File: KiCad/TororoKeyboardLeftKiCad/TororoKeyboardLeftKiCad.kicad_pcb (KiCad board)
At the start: 2 copper layers, 142.1 x 99.2 mm, 97 parts, among them J1 MJ-4PP-9, SW1 SW_PUSH, SW10 SW_PUSH, SW11 SW_PUSH, SW12 SW_PUSH, SW13 SW_PUSH, SW14 SW_PUSH, SW15 SW_PUSH, SW16 SW_PUSH, SW17 SW_PUSH, SW18 SW_PUSH, SW19 SW_PUSH, SW2 SW_PUSH, SW20 SW_PUSH, SW21 SW_PUSH, SW22 SW_PUSH, SW23 SW_PUSH, SW24 SW_PUSH, SW25 SW_PUSH, SW26 SW_PUSH, SW27 SW_PUSH, SW28 SW_PUSH, SW29 SW_PUSH, SW3 SW_PUSH, SW4 SW_PUSH, SW5 SW_PUSH, SW6 SW_PUSH, SW7 SW_PUSH, SW8 SW_PUSH, SW9 SW_PUSH, U1 ProMicro

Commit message: レイアウトを微調整
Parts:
- moved U1 0.30 mm to (51.1, 46.4)
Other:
- board size 142.1 x 99.2 mm -> 139.7 x 99.2 mm
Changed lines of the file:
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@@
   (general
     (thickness 1.6)
-    (drawings 266)
+    (drawings 268)
     (tracks 0)
     (zones 0)
@@
     (add_net row5)
   )
+  (module kbd_tororo:Hybrid_PCB_100H_no-silk_no_ref (layer F.Cu)
+    (at 66.675 47.625)
+    (fp_text reference SW2 (at 0 3.175) (layer F.SilkS) hide
+      (effects (font (size 1.27 1.524) (thickness 0.2032)))
+    )
+    (fp_text value SW_PUSH (at 0 5.08) (layer F.SilkS) hide
+      (effects (font (size 1.27 1.524) (thickness 0.2032)))
+    )
+    (fp_line (start -6.985 6.985) (end -6.985 -6.985) (layer Eco2.User) (width 0.1524))
+    (fp_line (start 6.985 6.985) (end -6.985 6.985) (layer Eco2.User) (width 0.1524))
+    (fp_line (start 6.985 -6.985) (end 6.985 6.985) (layer Eco2.User) (width 0.1524))
+    (fp_line (start -6.985 -6.985) (end 6.985 -6.985) (layer Eco2.User) (width 0.1524))
+    (fp_line (start -9.398 9.398) (end -9.398 -9.398) (layer Dwgs.User) (width 0.1524))
+    (fp_line (start 9.398 9.398) (end -9.398 9.398) (layer Dwgs.User) (width 0.1524))
+    (fp_line (start 9.398 -9.398) (end 9.398 9.398) (layer Dwgs.User) (width 0.1524))
+    (fp_line (start -9.398 -9.398) (end 9.398 -9.398) (layer Dwgs.User) (width 0.1524))
+    (fp_line (start -6.35 6.35) (end -6.35 -6.35) (layer Cmts.User) (width 0.1524))
+    (fp_line (start 6.35 6.35) (end -6.35 6.35) (layer Cmts.User) (width 0.1524))
+    (fp_line (start 6.35 -6.35) (end 6.35 6.35) (layer Cmts.User) (width 0.1524))
+    (fp_line (start -6.35 -6.35) (end 6.35 -6.35) (layer Cmts.User) (width 0.1524))
+    (fp_text user 1.00u (at -5.715 8.255) (layer Dwgs.User) hide
+      (effects (font (size 1.524 1.524) (thickness 0.3048)))
+    )
+    (pad 1 thru_hole oval (at -3.155 -3.27 138.1) (size 2.5 4.461556) (drill 0.001) (layers *.Cu *.Mask)
+      (net 71 col2))
+    (pad 1 thru_hole circle (at -3.81 -2.54 330.95) (size 2 2) (drill 1.524) (layers *.Cu *.Mask)
+      (net 71 col2))
+    (pad "" np_thru_hole circle (at 5.08 0 90) (size 1.8 1.8) (drill 1.8) (layers *.Cu *.Mask))
+    (pad "" np_thru_hole circle (at -5.08 0 90) (size 1.8 1.8) (drill 1.8) (layers *.Cu *.Mask))
+    (pad "" np_thru_hole circle (at 0 0 90) (size 3.9878 3.9878) (drill 3.9878) (layers *.Cu *.Mask))
+    (pad 1 thru_hole circle (at -2.5 -4 330.95) (size 2 2) (drill 1.524) (layers *.Cu *.Mask)
+      (net 71 col2))
+    (pad 2 thru_hole circle (at 2.54 -5.08 330.95) (size 2 2) (drill 1.524) (layers *.Cu *.Mask)
+      (net 3 "Net-(D2-Pad2)"))
+    (pad 2 thru_hole circle (at 2.5 -4.5 330.95) (size 2 2) (drill 1.524) (layers *.Cu *.Mask)
+      (net 3 "Net-(D2-Pad2)"))
+    (pad 2 thru_hole oval (at 2.52 -4.79 356.055) (size 2.5 3.081378) (drill 0.001) (layers *.Cu *.Mask)
+      (net 3 "Net-(D2-Pad2)"))
+  )
   (module kbd:HOLE (layer F.Cu)
     (at 157.1625 114.3)
@@
   )
   (module kbd_tororo:Hybrid_PCB_100H_no-silk_no_ref (layer F.Cu)
-    (at 66.675 47.625)
-    (fp_text reference SW2 (at 0 3.175) (layer F.SilkS) hide
-      (effects (font (size 1.27 1.524) (thickness 0.2032)))
-    )
-    (fp_text value SW_PUSH (at 0 5.08) (layer F.SilkS) hide
-      (effects (font (size 1.27 1.524) (thickness 0.2032)))
-    )
-    (fp_line (start -6.985 6.985) (end -6.985 -6.985) (layer Eco2.User) (width 0.1524))
-    (fp_line (start 6.985 6.985) (end -6.985 6.985) (layer Eco2.User) (width 0.1524))
-    (fp_line (start 6.985 -6.985) (end 6.985 6.985) (layer Eco2.User) (width 0.1524))
-    (fp_line (start -6.985 -6.985) (end 6.985 -6.985) (layer Eco2.User) (width 0.1524))
-    (fp_line (start -9.398 9.398) (end -9.398 -9.398) (layer Dwgs.User) (width 0.1524))
-    (fp_line (start 9.398 9.398) (end -9.398 9.398) (layer Dwgs.User) (width 0.1524))
-    (fp_line (start 9.398 -9.398) (end 9.398 9.398) (layer Dwgs.User) (width 0.1524))
-    (fp_line (start -9.398 -9.398) (end 9.398 -9.398) (layer Dwgs.User) (width 0.1524))
-    (fp_line (start -6.35 6.35) (end -6.35 -6.35) (layer Cmts.User) (width 0.1524))
-    (fp_line (start 6.35 6.35) (end -6.35 6.35) (layer Cmts.User) (width 0.1524))
-    (fp_line (start 6.35 -6.35) (end 6.35 6.35) (layer Cmts.User) (width 0.1524))
-    (fp_line (start -6.35 -6.35) (end 6.35 -6.35) (layer Cmts.User) (width 0.1524))
-    (fp_text user 1.00u (at -5.715 8.255) (layer Dwgs.User) hide
-      (effects (font (size 1.524 1.524) (thickness 0.3048)))
-    )
-    (pad 1 thru_hole oval (at -3.155 -3.27 138.1) (size 2.5 4.461556) (drill 0.001) (layers *.Cu *.Mask)
-      (net 71 col2))
-    (pad 1 thru_hole circle (at -3.81 -2.54 330.95) (size 2 2) (drill 1.524) (layers *.Cu *.Mask)
-      (net 71 col2))
-    (pad "" np_thru_hole circle (at 5.08 0 90) (size 1.8 1.8) (drill 1.8) (layers *.Cu *.Mask))
-    (pad "" np_thru_hole circle (at -5.08 0 90) (size 1.8 1.8) (drill 1.8) (layers *.Cu *.Mask))
-    (pad "" np_thru_hole circle (at 0 0 90) (size 3.9878 3.9878) (drill 3.9878) (layers *.Cu *.Mask))
-    (pad 1 thru_hole circle (at -2.5 -4 330.95) (size 2 2) (drill 1.524) (layers *.Cu *.Mask)
-      (net 71 col2))
-    (pad 2 thru_hole circle (at 2.54 -5.08 330.95) (size 2 2) (drill 1.524) (layers *.Cu *.Mask)
-      (net 3 "Net-(D2-Pad2)"))
-    (pad 2 thru_hole circle (at 2.5 -4.5 330.95) (size 2 2) (drill 1.524) (layers *.Cu *.Mask)
-      (net 3 "Net-(D2-Pad2)"))
-    (pad 2 thru_hole oval (at 2.52 -4.79 356.055) (size 2.5 3.081378) (drill 0.001) (layers *.Cu *.Mask)
-      (net 3 "Net-(D2-Pad2)"))
-  )
-  (module kbd_tororo:Hybrid_PCB_100H_no-silk_no_ref (layer F.Cu)
     (at 52.3875 66.675)
     (fp_text reference SW3 (at 0 3.175) (layer F.SilkS) hide
@@
   )
   (module kbd_tororo:ProMicro_v2_back (layer F.Cu)
-    (at 51.1 46.7 90)
+    (at 51.1 46.4 90)
     (fp_text reference U1 (at -1.27 2.762 180) (layer F.SilkS) hide
       (effects (font (size 1 1) (thickness 0.15)))
@@
       (net 77 "Net-(U1-Pad24)"))
   )
-  (gr_line (start 34.1 57.1) (end 34.1 39.1) (layer Edge.Cuts) (width 0.05))
-  (gr_line (start 38.1 57.1) (end 34.1 57.1) (layer Edge.Cuts) (width 0.05))
-  (gr_line (start 38.1 114.3) (end 38.1 57.1) (layer Edge.Cuts) (width 0.05))
+  (gr_line (start 38 38.7) (end 36.5 38.7) (layer Edge.Cuts) (width 0.05))
+  (gr_line (start 38 38.1) (end 38 38.7) (layer Edge.Cuts) (width 0.05))
+  (gr_line (start 79.5 38.1) (end 171.4 38.1) (layer Edge.Cuts) (width 0.05))
+  (gr_line (start 79.5 34.1) (end 79.5 38.1) (layer Edge.Cuts) (width 0.05))
+  (gr_line (start 79.2 34.1) (end 79.5 34.1) (layer Edge.Cuts) (width 0.05))
+  (gr_line (start 38 38.1) (end 72.8 38.1) (layer Edge.Cuts) (width 0.05))
+  (gr_line (start 72.8 34.1) (end 72.8 38.1) (layer Edge.Cuts) (width 0.05))
+  (gr_line (start 73.2 34.1) (end 72.8 34.1) (layer Edge.Cuts) (width 0.05))
+  (gr_line (start 36.5 56.7) (end 38.1 56.7) (layer Edge.Cuts) (width 0.05))
+  (gr_line (start 36.5 38.7) (end 36.5 56.7) (layer Edge.Cuts) (width 0.05))
+  (gr_line (start 38.1 114.3) (end 38.1 56.7) (layer Edge.Cuts) (width 0.05))
   (gr_line (start 66.7 114.3) (end 38.1 114.3) (layer Edge.Cuts) (width 0.05))
   (gr_line (start 66.7 133.3) (end 66.7 114.3) (layer Edge.Cuts) (width 0.05))
@@
   (gr_line (start 171.4 57.1) (end 161.9 57.1) (layer Edge.Cuts) (width 0.05))
   (gr_line (start 171.4 38.1) (end 171.4 57.1) (layer Edge.Cuts) (width 0.05))
-  (gr_line (start 79.2 38.1) (end 171.4 38.1) (layer Edge.Cuts) (width 0.05))
-  (gr_line (start 79.2 34.1) (end 79.2 38.1) (layer Edge.Cuts) (width 0.05))
   (gr_line (start 73.2 34.1) (end 79.2 34.1) (layer Edge.Cuts) (width 0.05))
-  (gr_line (start 73.2 38.1) (end 73.2 34.1) (layer Edge.Cuts) (width 0.05))
-  (gr_line (start 38.1 38.1) (end 73.2 38.1) (layer Edge.Cuts) (width 0.05))
-  (gr_line (start 38.1 39.1) (end 38.1 38.1) (layer Edge.Cuts) (width 0.05))
-  (gr_line (start 34.1 39.1) (end 38.1 39.1) (layer Edge.Cuts) (width 0.05))
   (gr_line (start 166.662 95.25) (end 166.662 76.2) (layer Dwgs.User) (width 0.152))
   (gr_line (start 176.186999 95.25) (end 166.662 95.25) (layer Dwgs.User) (width 0.152))

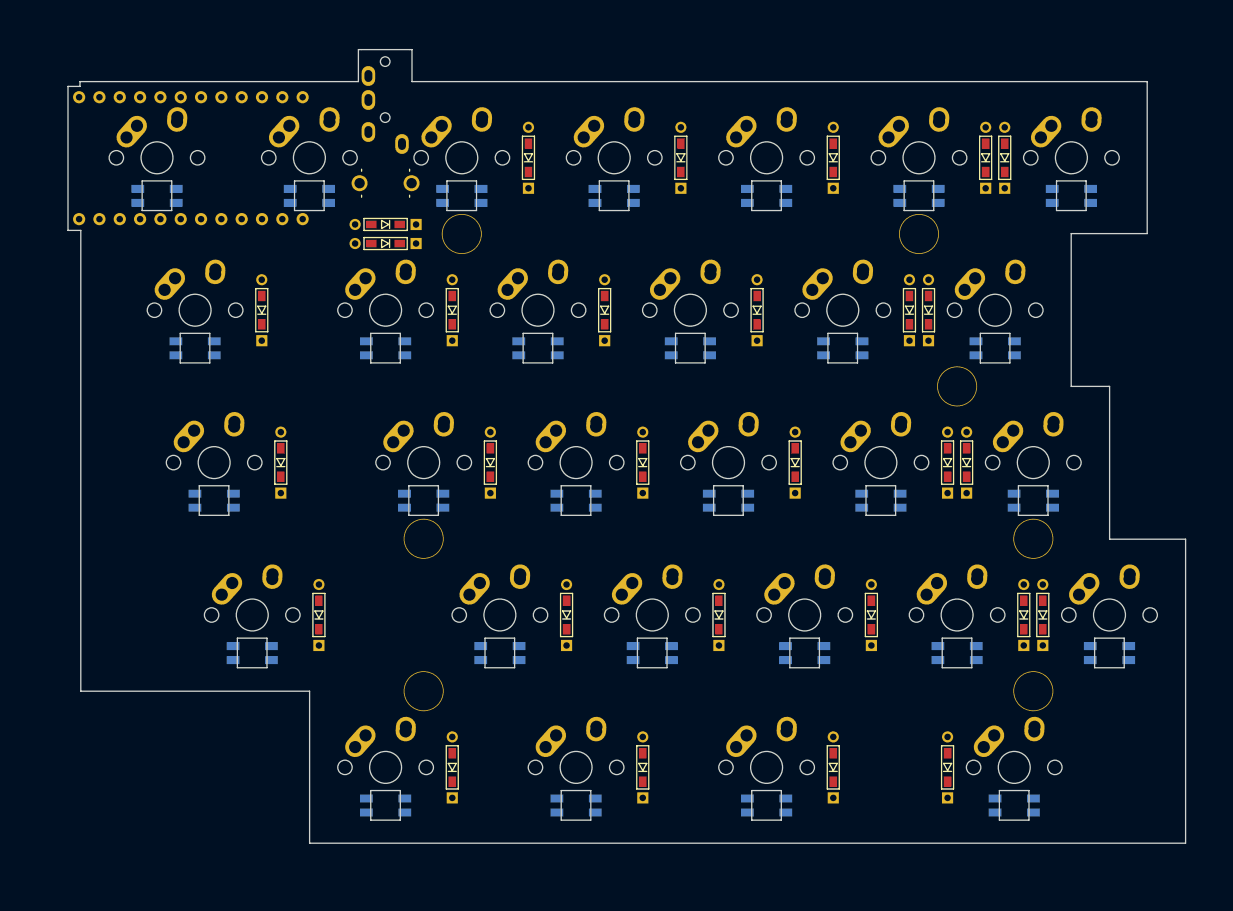
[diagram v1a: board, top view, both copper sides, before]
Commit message: 左手側の配線を整理
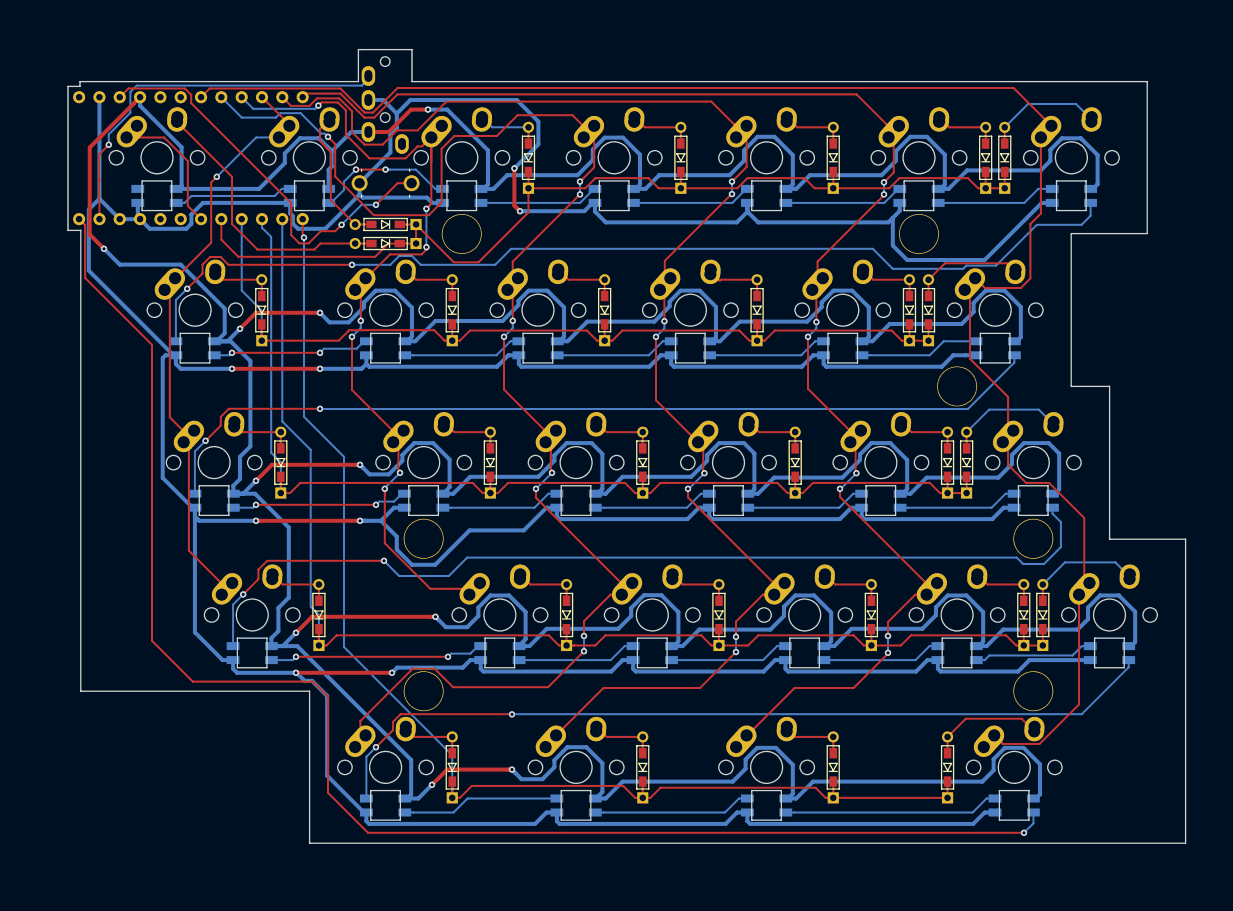
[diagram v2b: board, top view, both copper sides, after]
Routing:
- net VCC: track 0.00 -> 876.6 mm, vias 0 -> 10
- net GND: track 0.00 -> 718.1 mm, vias 0 -> 8
- net col7: track 0.00 -> 209.8 mm
- net led: track 0.00 -> 186.3 mm, vias 0 -> 1
- net col4: track 0.00 -> 181.3 mm, vias 0 -> 9
- net col6: track 0.00 -> 180.8 mm, vias 0 -> 8
- net col5: track 0.00 -> 174.6 mm, vias 0 -> 8
- net row4: track 0.00 -> 162.1 mm
- net row5: track 0.00 -> 152.4 mm, vias 0 -> 1
- net row3: track 0.00 -> 137.4 mm
- net Net-(L25-Pad3): track 0.00 -> 129.9 mm, vias 0 -> 2
- net row1: track 0.00 -> 127.4 mm
- net Net-(L27-Pad3): track 0.00 -> 119.9 mm, vias 0 -> 2
- net row2: track 0.00 -> 116.0 mm
- net Net-(L26-Pad3): track 0.00 -> 114.2 mm, vias 0 -> 2
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
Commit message: 表の塗りつぶしがうまく回るように配線を修正
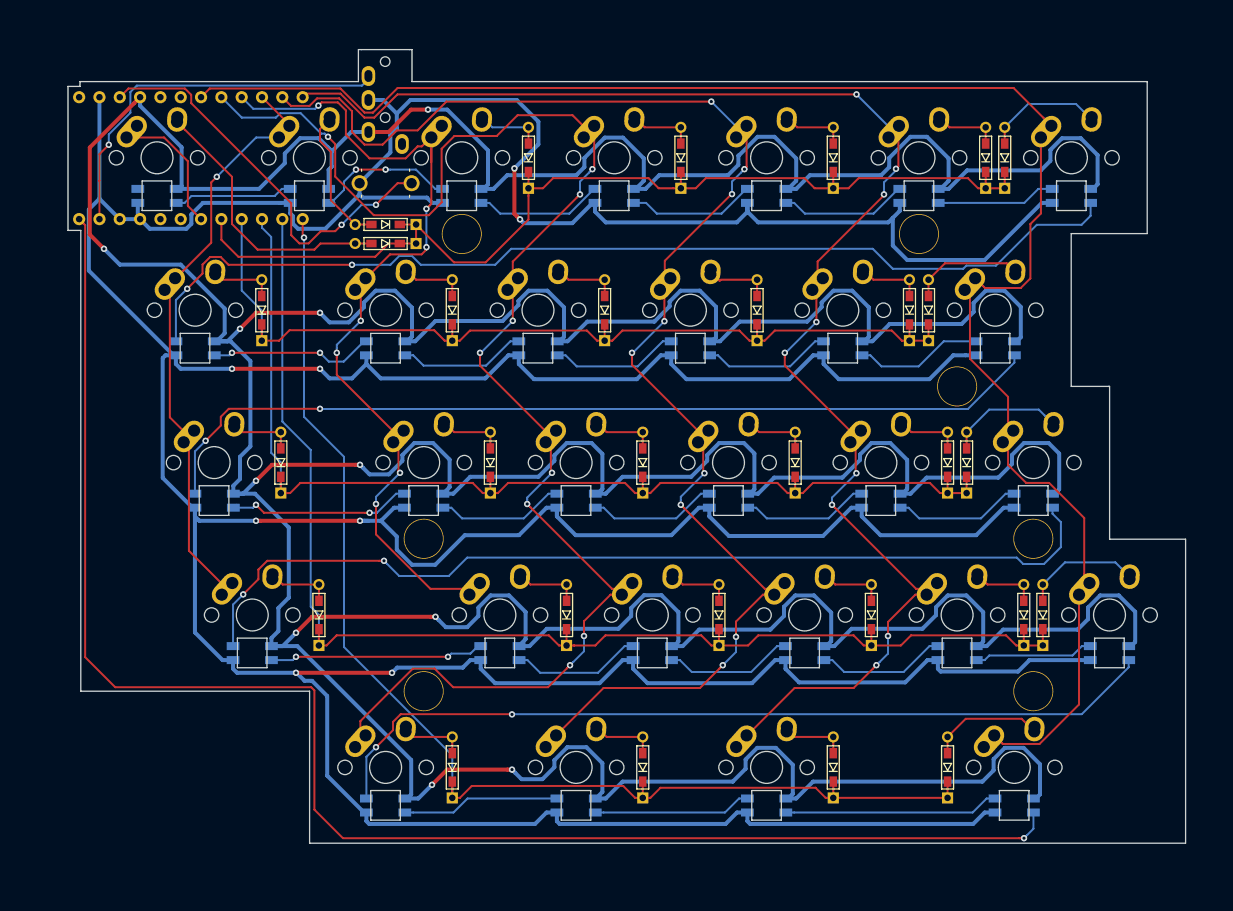
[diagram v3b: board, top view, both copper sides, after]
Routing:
- net GND: track 718.1 -> 734.6 mm
- net led: track 186.3 -> 195.0 mm
- net col6: track 180.8 -> 185.7 mm, vias 8 -> 9
- net col4: track 181.3 -> 185.9 mm
- net col5: track 174.6 -> 178.9 mm, vias 8 -> 9
- net col3: track 108.5 -> 111.0 mm
- net Net-(L13-Pad1): track 15.0 -> 16.3 mm
- net Net-(L13-Pad3): track 15.0 -> 16.2 mm
- net Net-(L18-Pad3): track 15.0 -> 16.2 mm
- net Net-(L21-Pad3): track 15.0 -> 16.1 mm
- net Net-(L16-Pad3): track 15.0 -> 16.1 mm
- net Net-(L11-Pad3): track 15.0 -> 16.1 mm
- net Net-(L12-Pad3): track 15.0 -> 16.1 mm
- net Net-(L17-Pad3): track 15.0 -> 16.1 mm
- net Net-(L22-Pad3): track 15.0 -> 16.1 mm
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
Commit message: 裏の塗りつぶしがうまく回るように配線を修正
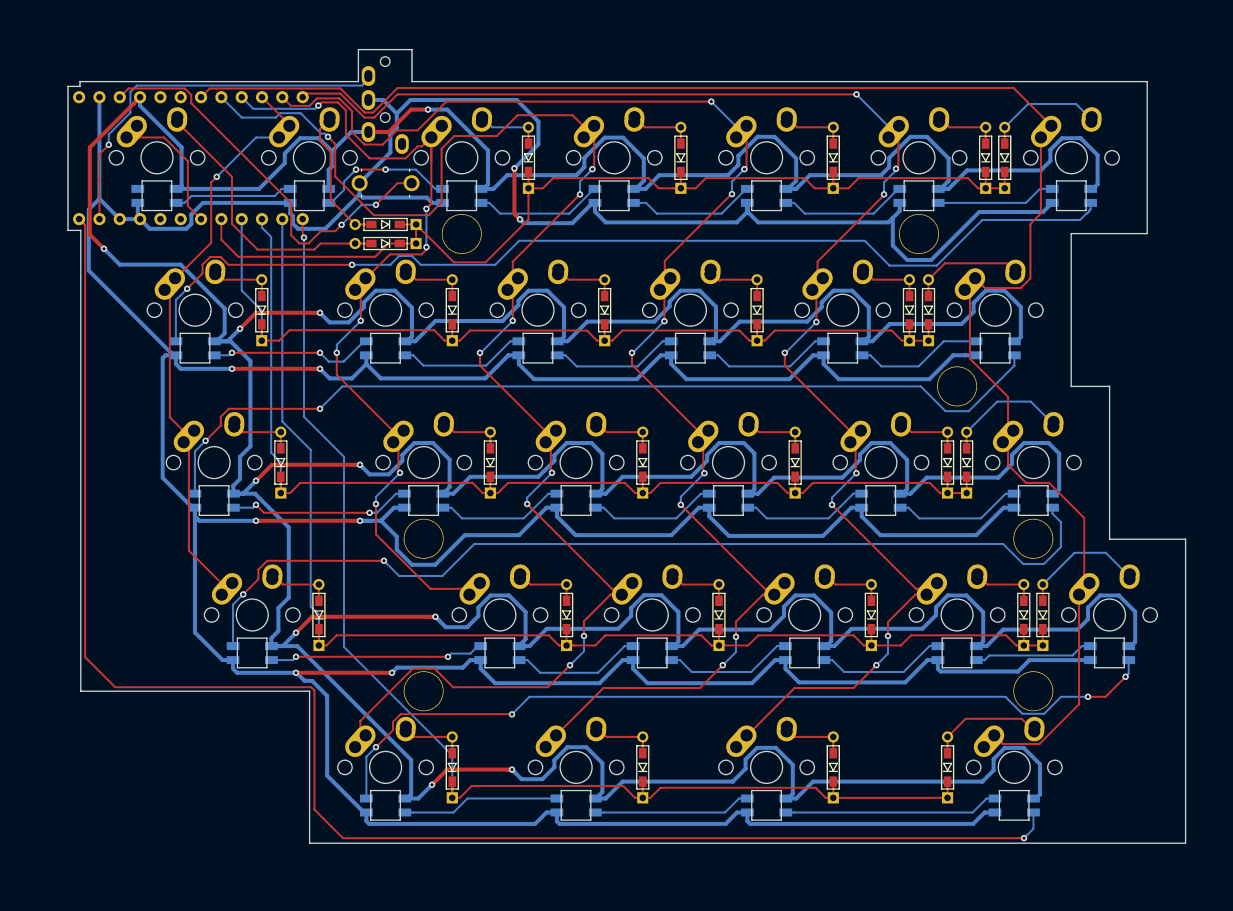
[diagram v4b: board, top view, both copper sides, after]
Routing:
- net Net-(L26-Pad3): track 114.2 -> 117.0 mm
- net Net-(L14-Pad1): track 106.7 -> 108.9 mm, vias 2 -> 4
- net Net-(L27-Pad3): track 119.9 -> 121.4 mm
- net Net-(D28-Pad2): track 14.8 -> 15.8 mm
- net Net-(D27-Pad2): track 14.8 -> 15.6 mm

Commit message: DRCに指摘されたのでパッドとの距離を調整
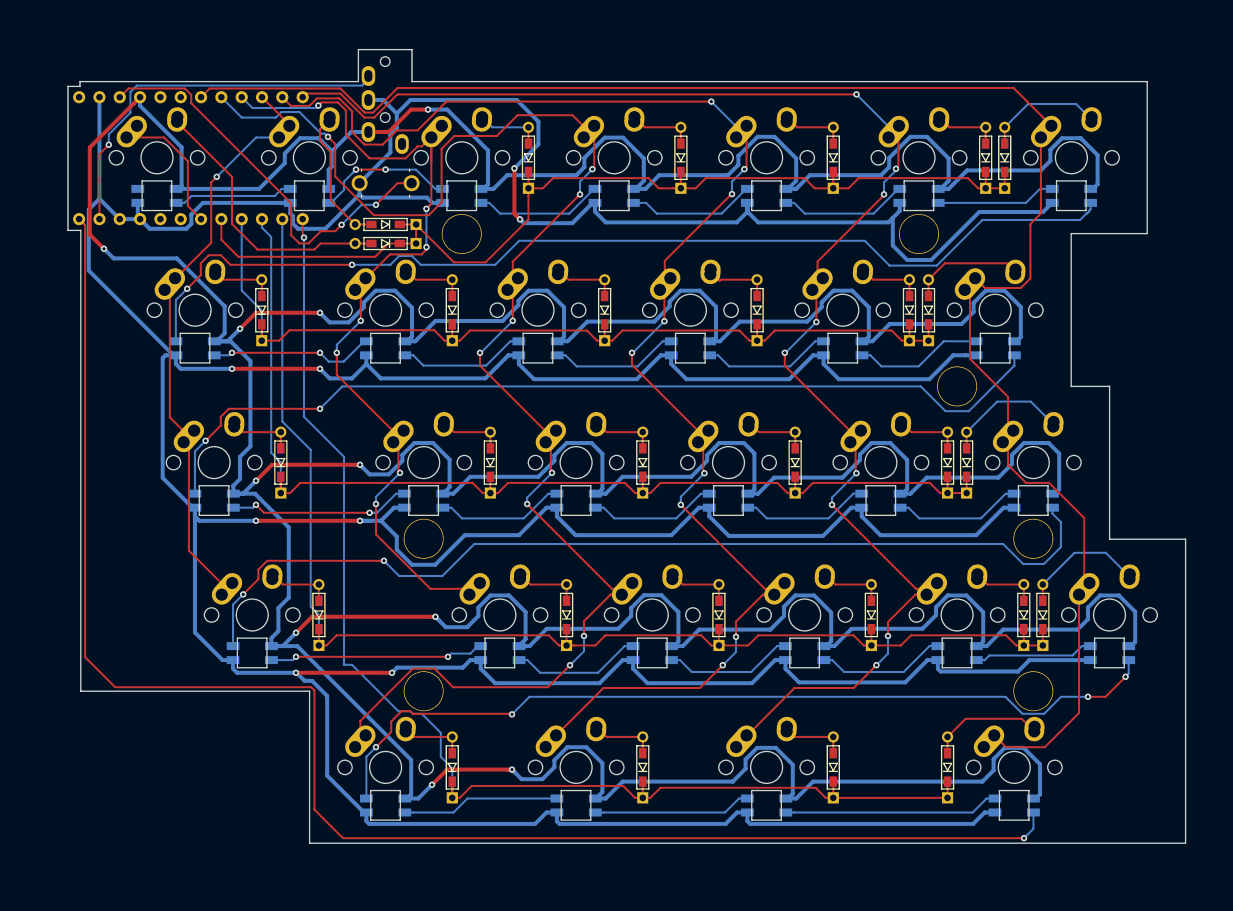
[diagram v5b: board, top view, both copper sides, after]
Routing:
- net row5: track 152.4 -> 154.5 mm
- net col7: track 209.8 -> 210.8 mm
